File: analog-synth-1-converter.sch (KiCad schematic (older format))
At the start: 12 parts, among them U1 TL084

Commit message: Annotate components
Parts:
- gave numbers to parts that had none: 11
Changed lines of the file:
@@
 $EndDescr
 $Comp
-L Transistor_BJT:2N3904 Q?
+L Transistor_BJT:2N3904 Q3
 U 1 1 5C89B3C5
 P 3450 3400
-F 0 "Q?" H 3641 3446 50  0000 L CNN
+F 0 "Q3" H 3641 3446 50  0000 L CNN
 F 1 "2N3904" H 3641 3355 50  0000 L CNN
 F 2 "Package_TO_SOT_THT:TO-92_Inline" H 3650 3325 50  0001 L CIN
@@
 $EndComp
 $Comp
-L Transistor_BJT:2N3904 Q?
+L Transistor_BJT:2N3904 Q4
 U 1 1 5C89B4F1
 P 4700 3400
-F 0 "Q?" H 4891 3446 50  0000 L CNN
+F 0 "Q4" H 4891 3446 50  0000 L CNN
 F 1 "2N3904" H 4891 3355 50  0000 L CNN
 F 2 "Package_TO_SOT_THT:TO-92_Inline" H 4900 3325 50  0001 L CIN
@@
 CV
 $Comp
-L Device:R R?
+L Device:R R6
 U 1 1 5C89B5B0
 P 3550 2850
-F 0 "R?" H 3620 2896 50  0000 L CNN
+F 0 "R6" H 3620 2896 50  0000 L CNN
 F 1 "1M" H 3620 2805 50  0000 L CNN
 F 2 "" V 3480 2850 50  0001 C CNN
@@
 $EndComp
 $Comp
-L power:+5V #PWR?
+L power:+5V #PWR023
 U 1 1 5C89B68B
 P 3550 2500
-F 0 "#PWR?" H 3550 2350 50  0001 C CNN
+F 0 "#PWR023" H 3550 2350 50  0001 C CNN
 F 1 "+5V" H 3565 2673 50  0000 C CNN
 F 2 "" H 3550 2500 50  0001 C CNN
@@
 	4600 3750 4600 3600
 $Comp
-L Device:R R?
+L Device:R R7
 U 1 1 5C89B709
 P 4100 4200
-F 0 "R?" H 4170 4246 50  0000 L CNN
+F 0 "R7" H 4170 4246 50  0000 L CNN
 F 1 "1k" H 4170 4155 50  0000 L CNN
 F 2 "" V 4030 4200 50  0001 C CNN
@@
 	4100 4650 4100 4350
 $Comp
-L Device:C C?
+L Device:C C7
 U 1 1 5C89BA5A
 P 3250 4150
-F 0 "C?" V 2998 4150 50  0000 C CNN
+F 0 "C7" V 2998 4150 50  0000 C CNN
 F 1 "1nf" V 3089 4150 50  0000 C CNN
 F 2 "" H 3288 4000 50  0001 C CNN
@@
 	2600 4150 2600 4550
 $Comp
-L power:GND #PWR?
+L power:GND #PWR022
 U 1 1 5C89C1AD
 P 2600 4900
-F 0 "#PWR?" H 2600 4650 50  0001 C CNN
+F 0 "#PWR022" H 2600 4650 50  0001 C CNN
 F 1 "GND" H 2605 4727 50  0000 C CNN
 F 2 "" H 2600 4900 50  0001 C CNN
@@
 	2600 4750 2950 4750
 $Comp
-L power:GND #PWR?
+L power:GND #PWR024
 U 1 1 5C89C3D6
 P 5100 3550
-F 0 "#PWR?" H 5100 3300 50  0001 C CNN
+F 0 "#PWR024" H 5100 3300 50  0001 C CNN
 F 1 "GND" H 5105 3377 50  0000 C CNN
 F 2 "" H 5100 3550 50  0001 C CNN
@@
 	5500 3600 5750 3600
 $Comp
-L Device:R_POT_TRIM RV?
+L Device:R_POT_TRIM RV3
 U 1 1 5C89D0E0
 P 6050 4050
-F 0 "RV?" V 5843 4050 50  0000 C CNN
+F 0 "RV3" V 5843 4050 50  0000 C CNN
 F 1 "100k" V 5934 4050 50  0000 C CNN
 F 2 "" H 6050 4050 50  0001 C CNN
@@
 $EndComp
 $Comp
-L Device:R R?
+L Device:R R10
 U 1 1 5C8A61D3
 P 7700 3850
-F 0 "R?" V 7493 3850 50  0000 C CNN
+F 0 "R10" V 7493 3850 50  0000 C CNN
 F 1 "10k" V 7584 3850 50  0000 C CNN
 F 2 "" V 7630 3850 50  0001 C CNN
@@
 $EndComp
 $Comp
-L Device:R R?
+L Device:R R9
 U 1 1 5C8A625A
 P 7300 4200
-F 0 "R?" H 7370 4246 50  0000 L CNN
+F 0 "R9" H 7370 4246 50  0000 L CNN
 F 1 "10k" H 7370 4155 50  0000 L CNN
 F 2 "" V 7230 4200 50  0001 C CNN
@@
 	8100 3350 8000 3350
 $Comp
-L power:GND #PWR?
+L power:GND #PWR027
 U 1 1 5C8A7985
 P 7300 4450
-F 0 "#PWR?" H 7300 4200 50  0001 C CNN
+F 0 "#PWR027" H 7300 4200 50  0001 C CNN
 F 1 "GND" H 7305 4277 50  0000 C CNN
 F 2 "" H 7300 4450 50  0001 C CNN
@@
 	7300 4450 7300 4350
 $Comp
-L Device:R_POT_TRIM RV?
+L Device:R_POT_TRIM RV5
 U 1 1 5C8A8DB2
 P 6900 3250
-F 0 "RV?" H 6830 3296 50  0000 R CNN
+F 0 "RV5" H 6830 3296 50  0000 R CNN
 F 1 "10k" H 6830 3205 50  0000 R CNN
 F 2 "" H 6900 3250 50  0001 C CNN
@@
 $EndComp
 $Comp
-L Device:R R?
+L Device:R R8
 U 1 1 5C8A8E4D
 P 6900 2850
-F 0 "R?" H 6970 2896 50  0000 L CNN
+F 0 "R8" H 6970 2896 50  0000 L CNN
 F 1 "1k" H 6970 2805 50  0000 L CNN
 F 2 "" V 6830 2850 50  0001 C CNN
@@
 $EndComp
 $Comp
-L Device:R_POT_TRIM RV?
+L Device:R_POT_TRIM RV4
 U 1 1 5C8A8EB9
 P 6900 2450
-F 0 "RV?" V 6693 2450 50  0000 C CNN
+F 0 "RV4" V 6693 2450 50  0000 C CNN
 F 1 "10k" V 6784 2450 50  0000 C CNN
 F 2 "" H 6900 2450 50  0001 C CNN
@@
 $EndComp
 $Comp
-L power:+12V #PWR?
+L power:+12V #PWR025
 U 1 1 5C8A8FD1
 P 6600 2300
-F 0 "#PWR?" H 6600 2150 50  0001 C CNN
+F 0 "#PWR025" H 6600 2150 50  0001 C CNN
 F 1 "+12V" H 6615 2473 50  0000 C CNN
 F 2 "" H 6600 2300 50  0001 C CNN
@@
 Connection ~ 6600 3500
 $Comp
-L power:GND #PWR?
+L power:GND #PWR026
 U 1 1 5C8AD153
 P 7200 2600
-F 0 "#PWR?" H 7200 2350 50  0001 C CNN
+F 0 "#PWR026" H 7200 2350 50  0001 C CNN
 F 1 "GND" H 7205 2427 50  0000 C CNN
 F 2 "" H 7200 2600 50  0001 C CNN

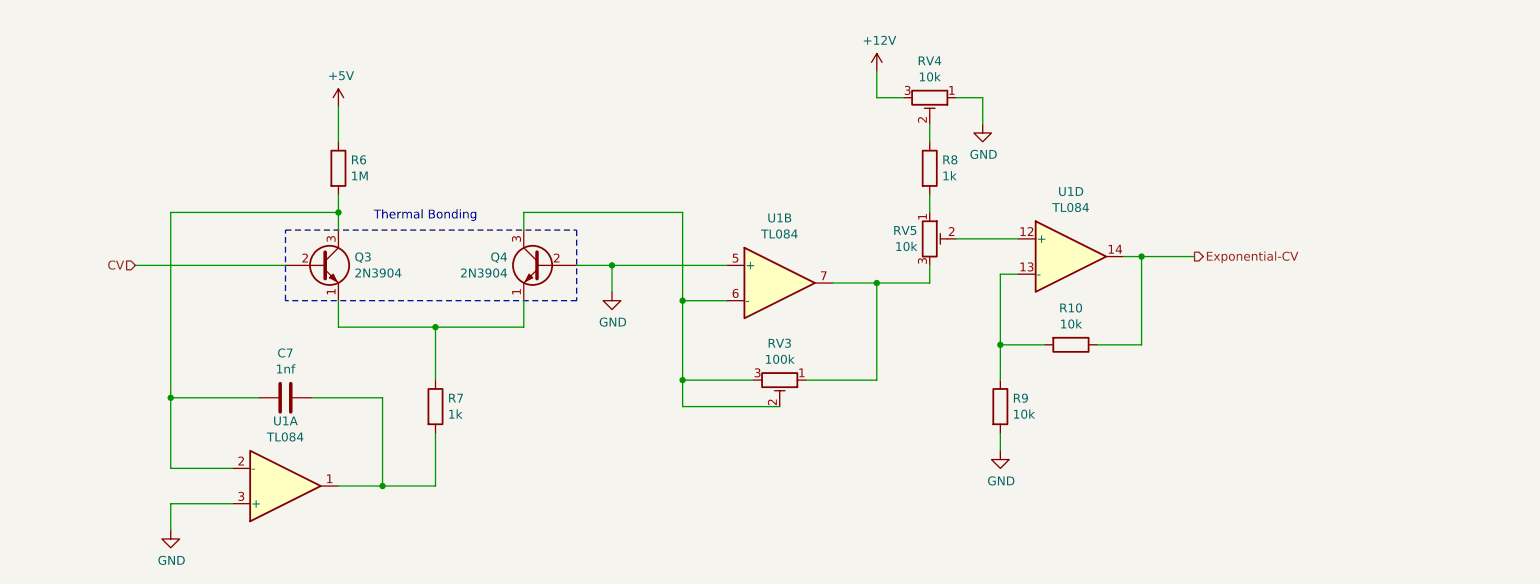
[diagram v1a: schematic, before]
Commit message: Add ATtiny85 overdrive protection, fix #5
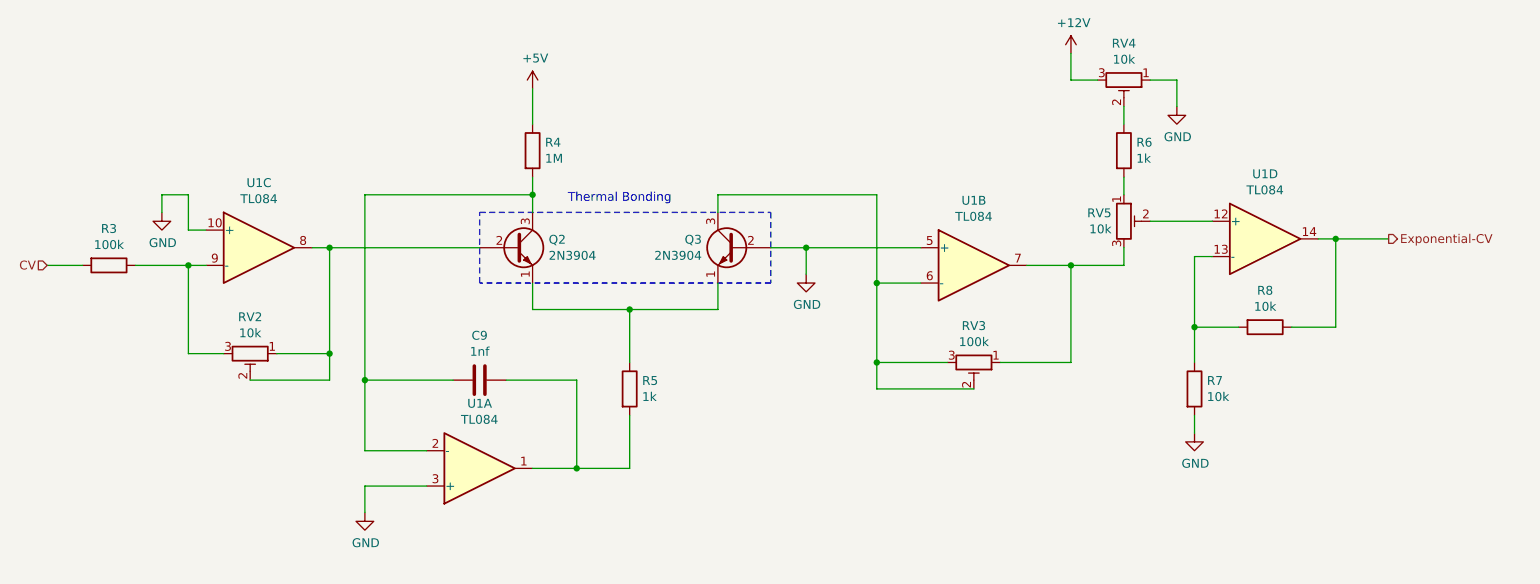
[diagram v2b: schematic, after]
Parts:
- added R3: 100k, symbol Device:R
- added RV2: 10k, symbol Device:R_POT_TRIM
- added unit 3 of U1
- renumbered C7 to C9, Q3 to Q2, Q4 to Q3, R6 to R4, R7 to R5, R8 to R6, R9 to R7, R10 to R8
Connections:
- net CV: now also R3.2; no longer Q2.2 (B)
- net GND: now also U1.10 (+)
- new net: Q2.2 (B), RV2.1, RV2.2, U1.8
- new net: R3.1, RV2.3, U1.9 (-)
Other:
- moved on the sheet: C9, Q2, Q3, R4, R5, R6, R7, R8, RV3, RV4, RV5, U1A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
